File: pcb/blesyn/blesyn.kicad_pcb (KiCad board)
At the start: 2 copper layers, 17.8 x 35.6 mm, 7 parts, among them J1 RJ12, U1 XIAO-ESP32-S3, U2 R-783.3-0.5

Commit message: move RJ12 50 mil away from esp32
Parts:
- moved J1 1.42 mm to (67.1, 120.9)
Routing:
- net /RX: track 38.5 -> 42.3 mm
- net GND: track 21.8 -> 23.2 mm
- net +12V: track 4.45 -> 5.87 mm
- net /TX: track 35.3 -> 36.2 mm
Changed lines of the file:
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@@
 	(footprint "Connector_RJ:RJ12_Amphenol_54601-x06_Horizontal"
 		(layer "F.Cu")
-		(at 67.07 122.29 180)
+		(at 67.07 120.87 180)
 		(descr "RJ12 6P6C horizontal socket, plastic body, tab down, https://cdn.amphenol-icc.com/media/wysiwyg/files/drawing/c-bmj-0082.pdf")
 		(tags "RJ12 connector")
@@
 		(layer "Edge.Cuts")
 	)
-	(dimension
-		(type orthogonal)
-		(layer "F.Fab")
-		(pts
-			(xy 55 147.54) (xy 75.32 147.54)
-		)
-		(height 7.62)
-		(orientation 0)
-		(format
-			(prefix "")
-			(suffix "")
-			(units 3)
-			(units_format 1)
-			(precision 4)
-		)
-		(style
-			(thickness 0.2)
-			(arrow_length 1.27)
-			(text_position_mode 0)
-			(arrow_direction outward)
-			(extension_height 0.58642)
-			(extension_offset 0.5)
-			(keep_text_aligned yes)
-		)
-		(gr_text "20,3200 mm"
-			(at 65.16 153.36 0)
-			(layer "F.Fab")
-			(effects
-				(font
-					(size 1.5 1.5)
-					(thickness 0.3)
-				)
-			)
-		)
-	)
-	(dimension
-		(type orthogonal)
-		(layer "F.Fab")
-		(pts
-			(xy 52.46 145) (xy 52.46 109.44)
-		)
-		(height -7.62)
-		(orientation 1)
-		(format
-			(prefix "")
-			(suffix "")
-			(units 3)
-			(units_format 1)
-			(precision 4)
-		)
-		(style
-			(thickness 0.2)
-			(arrow_length 1.27)
-			(text_position_mode 0)
-			(arrow_direction outward)
-			(extension_height 0.58642)
-			(extension_offset 0.5)
-			(keep_text_aligned yes)
-		)
-		(gr_text "35,5600 mm"
-			(at 43.04 127.22 90)
-			(layer "F.Fab")
-			(effects
-				(font
-					(size 1.5 1.5)
-					(thickness 0.3)
-				)
-			)
-		)
-	)
 	(segment
 		(start 56.27 128.49)
@@
 	)
 	(segment
-		(start 57.54 118.33)
-		(end 61.84 118.33)
+		(start 57.54 115.79)
+		(end 62.1755 115.79)
 		(width 0.4)
 		(layer "B.Cu")
@@
 	)
 	(segment
+		(start 56.27 125.95)
+		(end 56.27 117.06)
+		(width 0.4)
+		(layer "B.Cu")
+		(net "/RX")
+	)
+	(segment
 		(start 61.35 143.73)
 		(end 63.255 141.825)
@@
 	)
 	(segment
+		(start 56.27 117.06)
+		(end 57.54 115.79)
+		(width 0.4)
+		(layer "B.Cu")
+		(net "/RX")
+	)
+	(segment
 		(start 63.255 141.825)
 		(end 63.255 132.935)
@@
 	)
 	(segment
-		(start 56.27 125.95)
-		(end 56.27 119.6)
-		(width 0.4)
-		(layer "B.Cu")
-		(net "/RX")
-	)
-	(segment
-		(start 61.84 118.33)
-		(end 63.26 119.75)
-		(width 0.4)
-		(layer "B.Cu")
-		(net "/RX")
-	)
-	(segment
-		(start 56.27 119.6)
-		(end 57.54 118.33)
+		(start 63.26 116.8745)
+		(end 63.26 118.33)
+		(width 0.4)
+		(layer "B.Cu")
+		(net "/RX")
+	)
+	(segment
+		(start 62.1755 115.79)
+		(end 63.26 116.8745)
 		(width 0.4)
 		(layer "B.Cu")
@@
 	)
 	(segment
-		(start 70.39 119.75)
-		(end 65.8 119.75)
-		(width 0.4)
-		(layer "B.Cu")
-		(net "/TX")
-	)
-	(segment
 		(start 64.525 132.935)
 		(end 71.51 125.95)
@@
 	)
 	(segment
-		(start 71.51 120.87)
-		(end 70.39 119.75)
+		(start 71.51 120.235)
+		(end 69.605 118.33)
+		(width 0.4)
+		(layer "B.Cu")
+		(net "/TX")
+	)
+	(segment
+		(start 71.51 125.95)
+		(end 71.51 120.235)
+		(width 0.4)
+		(layer "B.Cu")
+		(net "/TX")
+	)
+	(segment
+		(start 69.605 118.33)
+		(end 65.8 118.33)
 		(width 0.4)
 		(layer "B.Cu")
@@
 	)
 	(segment
-		(start 71.51 125.95)
-		(end 71.51 120.87)
-		(width 0.4)
-		(layer "B.Cu")
-		(net "/TX")
-	)
-	(segment
 		(start 71.51 128.49)
 		(end 68.97 131.03)
@@
 	)
 	(segment
-		(start 61.99 122.78)
-		(end 63.89 124.68)
+		(start 61.99 120.87)
+		(end 61.99 122.145)
 		(width 0.4)
 		(layer "B.Cu")
@@
 	)
 	(segment
-		(start 63.89 124.68)
+		(start 63.89 124.045)
 		(end 63.89 125.95)
 		(width 0.4)
@@
 	)
 	(segment
-		(start 61.99 122.29)
-		(end 61.99 122.78)
+		(start 61.99 122.145)
+		(end 63.89 124.045)
 		(width 0.4)
 		(layer "B.Cu")
@@
 	)
 	(segment
-		(start 64.53 122.29)
-		(end 64.53 122.78)
+		(start 66.43 124.045)
+		(end 66.43 125.95)
 		(width 0.4)
 		(layer "B.Cu")
@@
 	)
 	(segment
-		(start 66.43 124.68)
-		(end 66.43 125.95)
+		(start 64.53 122.145)
+		(end 66.43 124.045)
 		(width 0.4)
 		(layer "B.Cu")
@@
 	)
 	(segment
-		(start 64.53 122.78)
-		(end 66.43 124.68)
-		(width 0.4)
-		(layer "B.Cu")
+		(start 64.53 120.87)
+		(end 64.53 122.145)
+		(width 0.4)
+		(layer "B.Cu")

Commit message: add SMD1206 handsoldering parts
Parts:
- added D3: BAT42, Diode_SMD:D_1206_3216Metric_Pad1.42x1.75mm_HandSolder, B.Cu at (58.8, 139.9)
- added D4: BAT42, Diode_SMD:D_1206_3216Metric_Pad1.42x1.75mm_HandSolder, B.Cu at (69.0, 139.9)
- added R3: 10k, Resistor_SMD:R_1206_3216Metric_Pad1.30x1.75mm_HandSolder, B.Cu at (61.4, 139.9)
- added R4: 10k, Resistor_SMD:R_1206_3216Metric_Pad1.30x1.75mm_HandSolder, B.Cu at (66.4, 139.7)
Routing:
- net GND: track 23.2 -> 13.5 mm
- net Net-(D1-K): track 11.2 -> 18.2 mm
- net Net-(D2-K): track 11.2 -> 17.8 mm
- net /TX: track 36.2 -> 40.8 mm
- net /RX: track 42.3 -> 46.7 mm

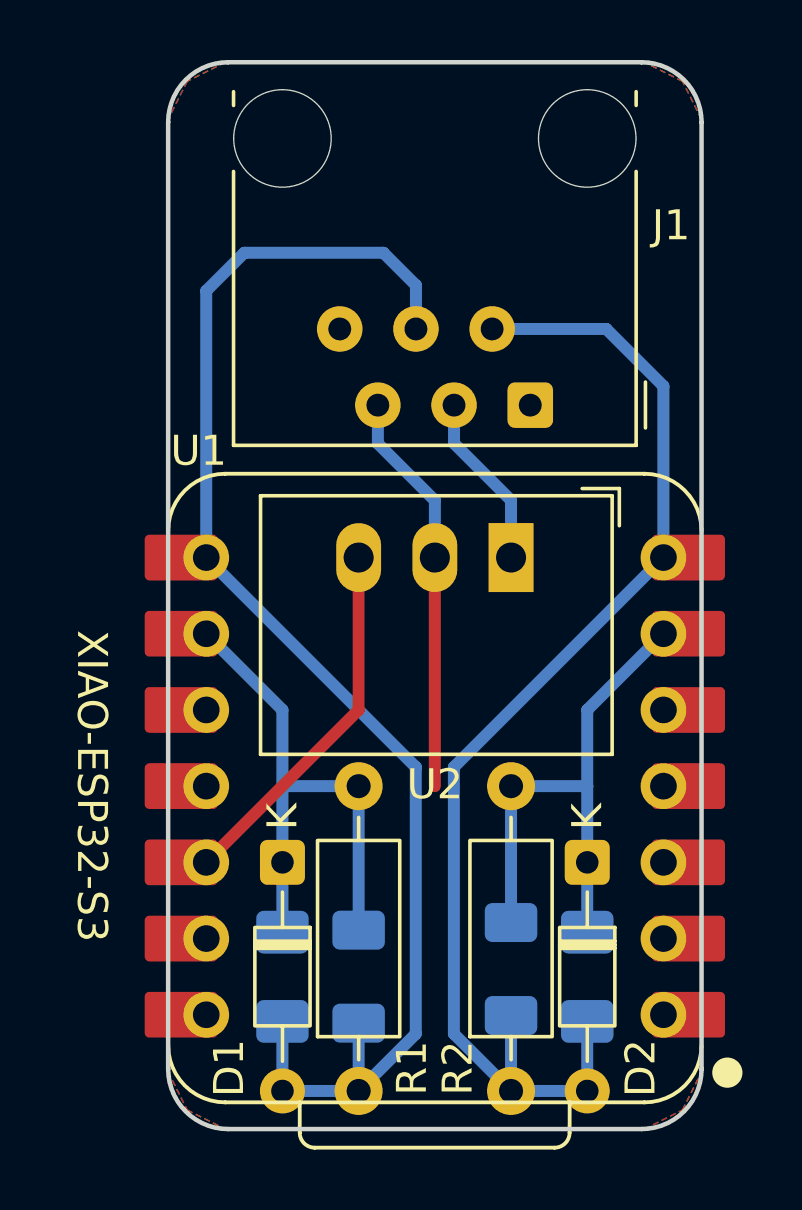
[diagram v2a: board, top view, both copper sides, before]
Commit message: align SMD resistor
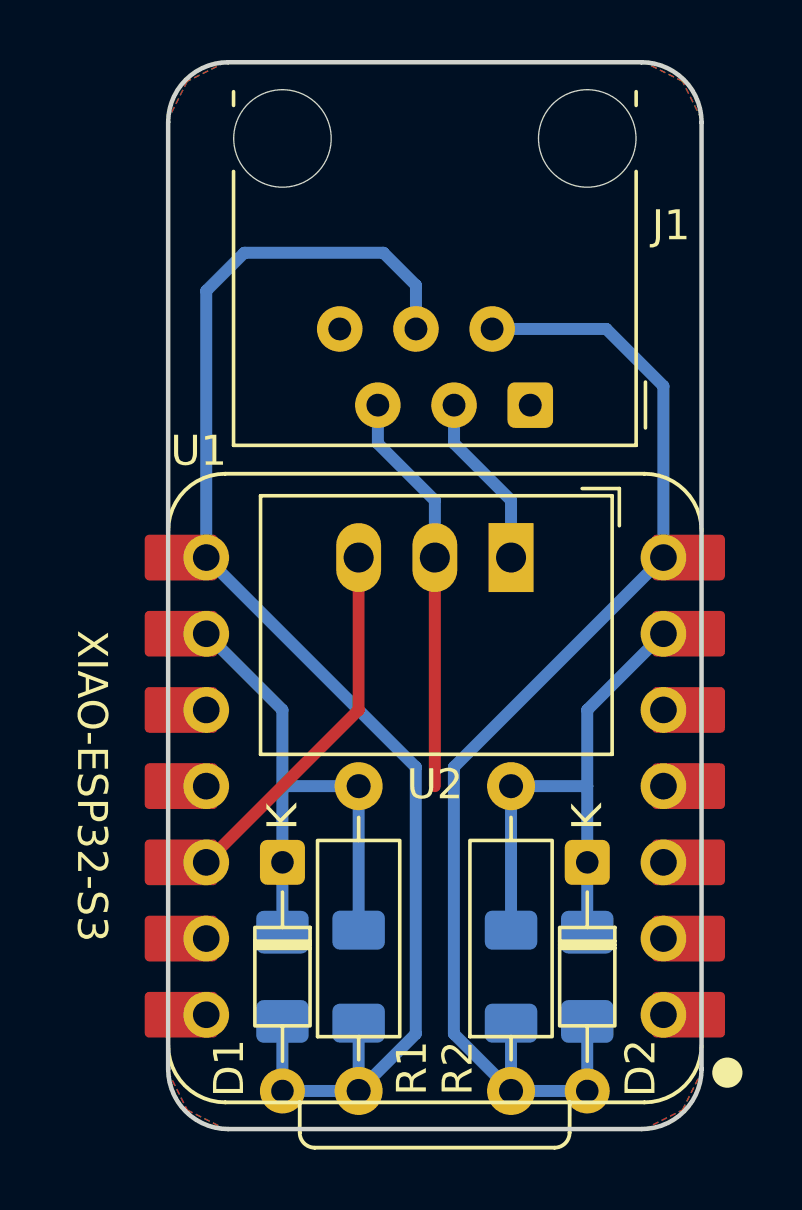
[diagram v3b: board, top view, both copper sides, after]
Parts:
- moved R4 0.25 mm to (66.4, 139.9)
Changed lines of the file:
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@@
 	(footprint "Resistor_SMD:R_1206_3216Metric_Pad1.30x1.75mm_HandSolder"
 		(layer "B.Cu")
-		(at 66.43 139.666 90)
+		(at 66.43 139.92 90)
 		(descr "Resistor SMD 1206 (3216 Metric), square (rectangular) end terminal, IPC-7351 nominal with elongated pad for handsoldering. (Body size source: IPC-SM-782 page 72, https://www.pcb-3d.com/wordpress/wp-content/uploads/ipc-sm-782a_amendment_1_and_2.pdf)")
 		(tags "resistor handsolder")
@@
 	)
 	(segment
+		(start 66.43 141.47)
+		(end 66.43 143.73)
+		(width 0.4)
+		(layer "B.Cu")
+		(net "/TX")
+	)
+	(segment
 		(start 66.43 143.73)
 		(end 68.97 143.73)
@@
 	)
 	(segment
-		(start 66.43 143.73)
-		(end 66.43 141.3285)
-		(width 0.4)
-		(layer "B.Cu")
-		(net "/TX")
-	)
-	(segment
 		(start 71.51 125.95)
 		(end 71.51 120.235)
@@
 	)
 	(segment
+		(start 66.43 133.57)
+		(end 66.43 138.37)
+		(width 0.4)
+		(layer "B.Cu")
+		(net "Net-(D2-K)")
+	)
+	(segment
 		(start 68.97 131.03)
 		(end 68.97 133.57)
@@
 		(width 0.4)
 		(layer "B.Cu")
-		(net "Net-(D2-K)")
-	)
-	(segment
-		(start 66.43 133.57)
-		(end 66.43 138.0035)
-		(width 0.4)
-		(layer "B.Cu")
